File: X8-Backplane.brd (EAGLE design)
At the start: 122.1 x 106.6 mm, 13 parts, among them IC1 MAX3467CPA, U2 MIC29501-5.0WU, U3 MIC29501-5.0WU

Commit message: added some new parts
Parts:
- added U$1: MAX3491, BackplaneParts:MAX3491
- added U$2: BD6221, HBridge:BD6221
- added U1: BD6221FSOP, CamSensComponents:SOP8
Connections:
- new net VCC: U1.2, U1.3
- net GND: now also U1.8
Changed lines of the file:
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@@
 <element name="C7" library="SparkFun-Passives" package="0603-CAP" value="10uF" x="111.9378" y="51.1048" rot="MR180"/>
 <element name="C8" library="SparkFun-Passives" package="0603-CAP" value="0.1uF" x="113.6396" y="49.5046" rot="MR0"/>
+<element name="U$1" library="BackplaneParts" package="MAX3491" value="MAX3491" x="-7.112" y="-66.7512"/>
+<element name="U1" library="CamSensComponents" package="SOP8" value="BD6221FSOP" x="-15.0114" y="-65.3796"/>
+<element name="U$2" library="HBridge" package="BD6221" value="BD6221" x="-21.1074" y="-65.7606"/>
 </elements>
 <signals>
@@
 <vertex x="123.7234" y="63.0174"/>
 </polygon>
+<contactref element="U1" pad="8"/>
+<wire x1="-3.2512" y1="-48.0822" x2="-14.4164" y2="-60.4296" width="0" layer="19" extent="1-1"/>
 <wire x1="101.1564" y1="49.276" x2="-3.2512" y2="-48.0822" width="0" layer="19" extent="1-16"/>
 </signal>
@@
 <contactref element="U$4" pad="66"/>
 </signal>
+<signal name="VCC">
+<contactref element="U1" pad="2"/>
+<contactref element="U1" pad="3"/>
+<wire x1="-11.8764" y1="-65.9296" x2="-13.1464" y2="-65.9296" width="0" layer="19" extent="1-1"/>
+</signal>
 </signals>

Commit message: finished adding components, added descriptions of pins
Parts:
- removed IC1: MAX3467CPA, maxim:SO08
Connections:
- removed net +3V3: IC1.1
- removed net COM_A: IC1.8
- removed net COM_B: IC1.7
- removed net COM_Y: IC1.5
- removed net COM_Z: IC1.6
- removed net TETHER_RX: IC1.2
- removed net TETHER_TX: IC1.3
- net GND: no longer IC1.4
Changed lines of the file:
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@@
 <element name="U$3" library="Other" package="BNO055" value="BNO055_9DOF_BREAKOUT" x="21.844" y="25.146"/>
 <element name="U$4" library="backplane_to_shield_connector" package="MA20-2" value="SHIELDCONNECTOR" x="60.706" y="40.894"/>
-<element name="IC1" library="maxim" package="SO08" value="MAX3467CPA" x="-5.1562" y="-45.0088">
-<attribute name="OC_NEWARK" value="unknown" x="-14.2494" y="-28.6258" size="1.778" layer="27" display="off"/>
-<attribute name="MPN" value="" x="-14.2494" y="-28.6258" size="1.778" layer="27" display="off"/>
-<attribute name="OC_FARNELL" value="unknown" x="-14.2494" y="-28.6258" size="1.778" layer="27" display="off"/>
-<attribute name="MF" value="" x="-14.2494" y="-28.6258" size="1.778" layer="27" display="off"/>
-</element>
 <element name="U$7" library="test_lib" package="MSOP_10" value="PCA9615" x="-7.9248" y="-54.991"/>
 <element name="U2" library="LDO" package="TO-263-5" value="MIC29501-5.0WU" x="101.1682" y="62.9158" rot="MR0">
@@
 </signal>
 <signal name="GND">
-<contactref element="IC1" pad="4"/>
 <contactref element="U2" pad="3"/>
 <contactref element="U3" pad="3"/>
@@
 </polygon>
 <contactref element="U1" pad="8"/>
-<wire x1="-3.2512" y1="-48.0822" x2="-14.4164" y2="-60.4296" width="0" layer="19" extent="1-1"/>
-<wire x1="101.1564" y1="49.276" x2="-3.2512" y2="-48.0822" width="0" layer="19" extent="1-16"/>
+<wire x1="101.1682" y1="65.659" x2="112.7506" y2="65.7098" width="0" layer="19" extent="16-16"/>
+<wire x1="112.7506" y1="53.9115" x2="112.7506" y2="65.7098" width="0" layer="19" extent="16-16"/>
+<wire x1="112.7878" y1="51.1048" x2="112.7506" y2="53.9115" width="0" layer="19" extent="16-16"/>
+<wire x1="112.7896" y1="49.5046" x2="112.7878" y2="51.1048" width="0" layer="19" extent="16-16"/>
+<wire x1="101.1682" y1="53.8607" x2="112.7506" y2="53.9115" width="0" layer="19" extent="16-16"/>
+<wire x1="101.1292" y1="51.0032" x2="101.1682" y2="53.8607" width="0" layer="19" extent="16-16"/>
+<wire x1="101.1564" y1="49.276" x2="101.1292" y2="51.0032" width="0" layer="19" extent="16-16"/>
+<wire x1="-14.4164" y1="-60.4296" x2="101.1564" y2="49.276" width="0" layer="19" extent="1-16"/>
 </signal>
 <signal name="+12V">
@@
 <contactref element="PCB1" pad="P$1"/>
 </signal>
-<signal name="+3V3">
-<contactref element="IC1" pad="1"/>
-</signal>
-<signal name="TETHER_RX">
-<contactref element="IC1" pad="2"/>
-</signal>
-<signal name="TETHER_TX">
-<contactref element="IC1" pad="3"/>
-</signal>
-<signal name="COM_A">
-<contactref element="IC1" pad="8"/>
-</signal>
-<signal name="COM_B">
-<contactref element="IC1" pad="7"/>
-</signal>
-<signal name="COM_Y">
-<contactref element="IC1" pad="5"/>
-</signal>
-<signal name="COM_Z">
-<contactref element="IC1" pad="6"/>
-</signal>
 <signal name="EN1">

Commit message: first draft of the sechematic. Almost there!
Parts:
- removed U$2: BD6221, HBridge:BD6221
- added U$5: AP2210, PowerComponents:SOT-23-3
- added U4, U5: FQB27P06, CamSensComponents:TO263-3
- moved U$7 112.4 mm to (13.3, 55.4), flipped to the bottom, turned to 270 degrees
- moved U$1 109.0 mm to (18.0, 39.3), flipped to the bottom
- moved U1 96.0 mm to (16.2, 25.5)
- moved U$3 37.4 mm to (22.0, 62.5), turned to 180 degrees
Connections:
- removed net N$4: PCB1.P$1
- removed net VCC: U1.2, U1.3
- new net !RE: PCB1.P$16, U$1.!RE
- new net 3.3V: U$1.VCC13, U$1.VCC14, U$3.VIN, U$5.VOUT, U$7.1, U$7.10
- new net 3V3_PIEZO: U$4.10, U$4.9, U1.1
- new net A: U$1.A, U$4.26
- new net B: U$1.B, U$4.24
- new net DE: PCB1.P$18, U$1.DE
- new net DSCLM: U$4.36, U$7.6
- new net DSCLP: U$4.35, U$7.7
- new net DSDAM: U$4.38, U$7.9
- new net DSDAP: U$4.37, U$7.8
- new net FIN: PCB1.P$33, U1.4
- new net GND_PIEZO: U$4.11, U$4.12, U1.7
- new net LASER_5V: U$4.57, U$4.58, U5.TAB
- new net LASER_ON: PCB1.P$29, U5.1
- new net LED_5V: U$4.59, U$4.60, U4.TAB
- new net LED_ON: PCB1.P$31, U4.1
- new net RIN: U1.5
- new net RX: PCB1.P$10, U$1.R0
- new net SCL: PCB1.P$5, U$3.SCL, U$4.39, U$7.4
- new net SDA: PCB1.P$3, U$3.SDA, U$4.40, U$7.2
- new net SERVO_PWM: PCB1.P$12, U$4.30
- new net TX: PCB1.P$8, U$1.DI
- new net Y: U$1.Y, U$4.20
- new net Z: U$1.Z, U$4.22
- net +12V: now also U$4.66, U$4.67, U$4.68, U1.2, U1.3, U1.6
- net +5V: now also PCB1.P$2, PCB1.P$4, U$5.VIN; no longer U$4.59, U$4.60, U$4.61, U$4.62
- net +5V_CAMERA_TUBE: now also U$4.53, U$4.54, U$4.55, U$4.56, U4.3, U5.3; no longer U$4.65, U$4.66, U$4.67, U$4.68
- net GND: now also PCB1.P$14, PCB1.P$20, PCB1.P$25, PCB1.P$30, PCB1.P$34, PCB1.P$39, PCB1.P$6, PCB1.P$9, U$1.GND6, U$1.GND7, U$3.GND, U$4.41, U$4.42, U$4.43, U$4.44, U$4.45, U$4.46, U$4.47, U$4.48, U$4.49, U$4.50, U$5.GND, U$7.5
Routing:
- added copper zone on layer 1, net GND
- removed copper zone on layer 16, net +5V
- removed copper zone on layer 16, net +5V_CAMERA_TUBE

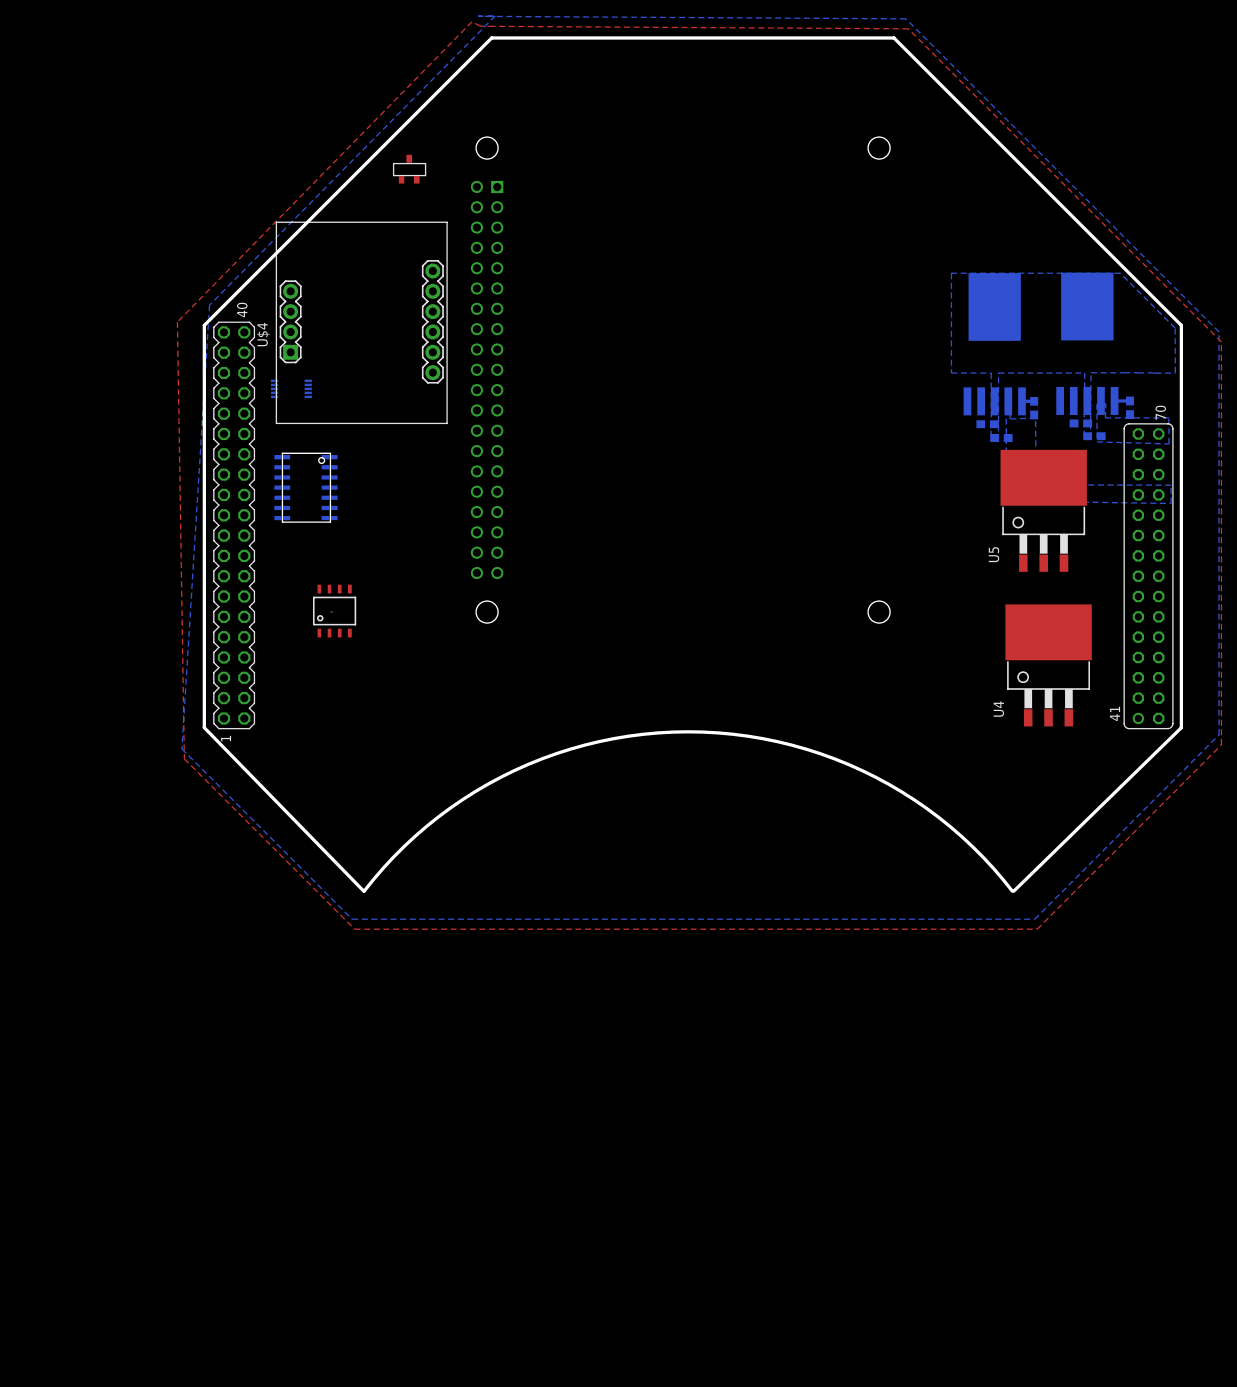
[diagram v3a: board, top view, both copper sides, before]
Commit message: Added a mosfet for an led for the blue tooth
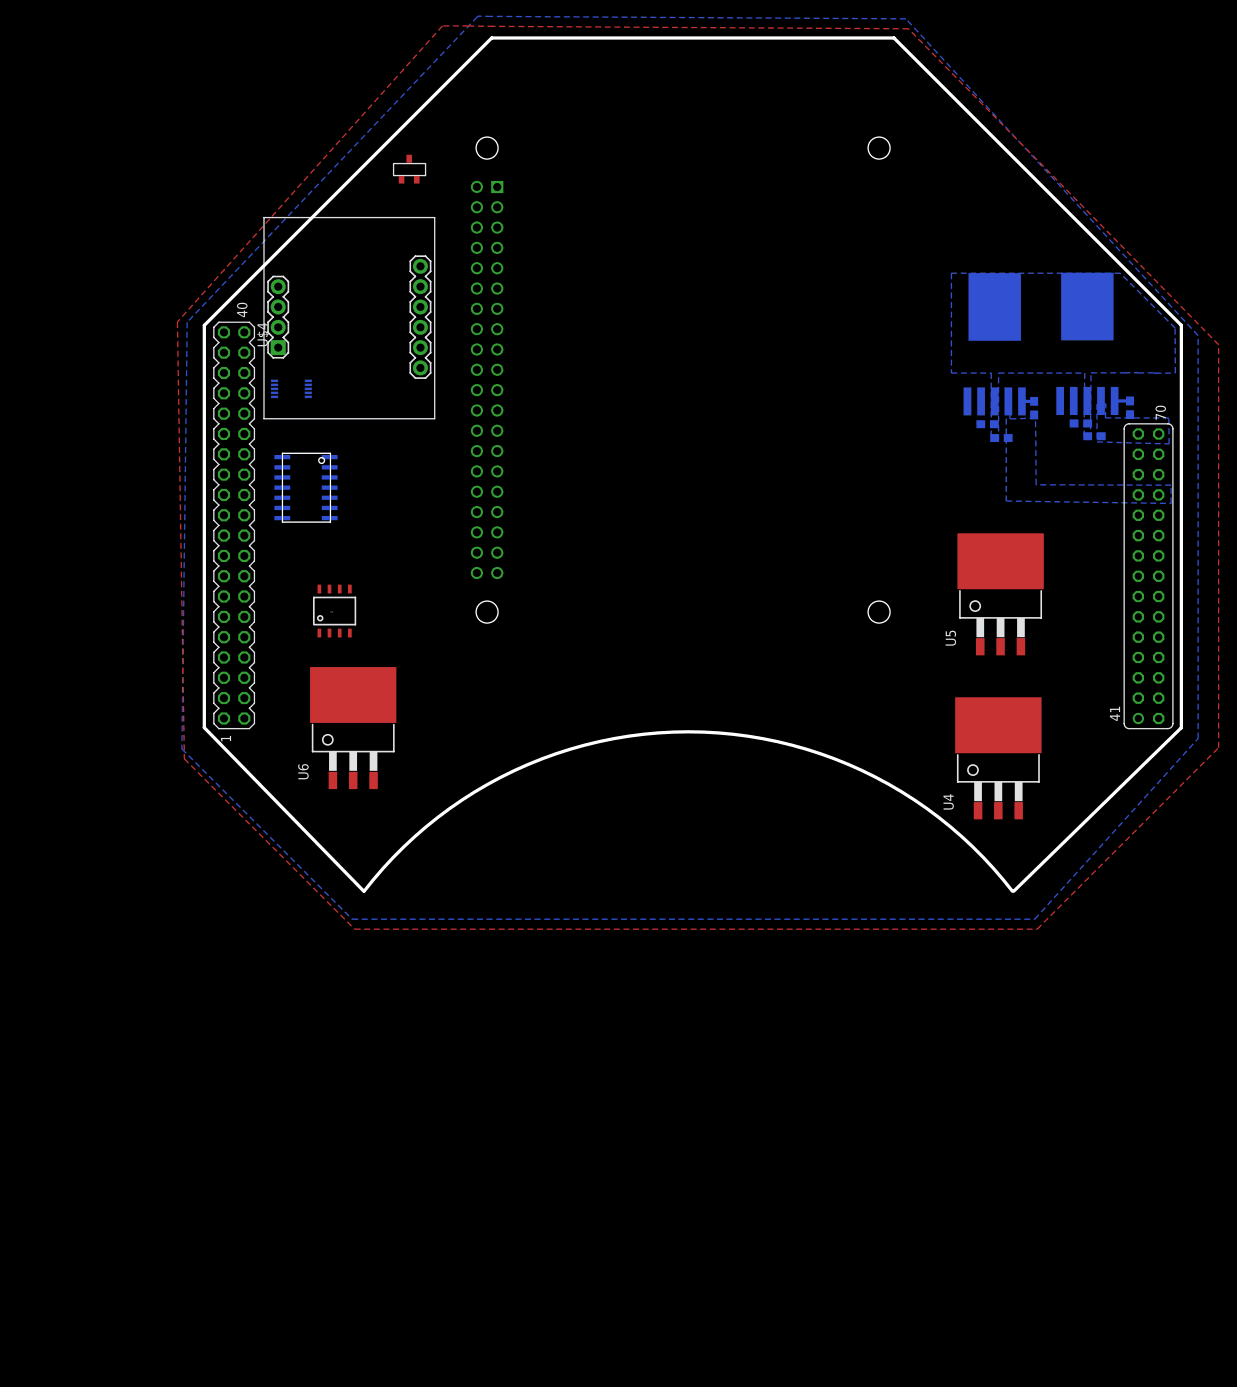
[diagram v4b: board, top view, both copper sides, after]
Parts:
- added U6: FQB27P06, CamSensComponents:TO263-3
- moved U4 13.2 mm to (101.6, 7.77)
- moved U5 11.7 mm to (101.9, 28.3)
- moved U$3 1.66 mm to (20.5, 63.1)
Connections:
- new net BT_LED_5V: U$4.15, U$4.16, U6.TAB
- new net BT_LED_ON: PCB1.P$36, U6.1
- net +5V_CAMERA_TUBE: now also U6.3
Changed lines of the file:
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@@
 <elements>
 <element name="PCB1" library="MicrocontrollerComponents" package="RPI2" value="RPI2" x="90.216" y="89.022" rot="MR270"/>
-<element name="U$3" library="Other" package="BNO055" value="BNO055_9DOF_BREAKOUT" x="22.0472" y="62.5348" rot="R180"/>
+<element name="U$3" library="Other" package="BNO055" value="BNO055_9DOF_BREAKOUT" x="20.4978" y="63.119" rot="R180"/>
 <element name="U$4" library="backplane_to_shield_connector" package="MA20-2" value="SHIELDCONNECTOR" x="60.706" y="40.894"/>
 <element name="U$7" library="test_lib" package="MSOP_10" value="PCA9615" x="13.2588" y="55.4228" rot="MR270"/>
@@
 <element name="U1" library="CamSensComponents" package="SOP8" value="BD6221FSOP" x="16.1544" y="25.4508"/>
 <element name="U$5" library="PowerComponents" package="SOT-23-3" value="AP2210" x="27.0256" y="81.5848"/>
-<element name="U4" library="CamSensComponents" package="TO263-3" value="FQB27P06" x="107.8992" y="19.3802"/>
-<element name="U5" library="CamSensComponents" package="TO263-3" value="FQB27P06" x="107.2896" y="38.7096"/>
+<element name="U4" library="CamSensComponents" package="TO263-3" value="FQB27P06" x="101.6254" y="7.7724"/>
+<element name="U5" library="CamSensComponents" package="TO263-3" value="FQB27P06" x="101.9048" y="28.2702"/>
+<element name="U6" library="CamSensComponents" package="TO263-3" value="FQB27P06" x="20.9804" y="11.557"/>
 </elements>
 <signals>
@@
 <polygon width="0.4064" layer="16">
 <vertex x="36.576" y="102.0064"/>
-<vertex x="38.735" y="102.0318"/>
-<vertex x="3.0226" y="65.8876"/>
+<vertex x="36.4998" y="101.9302"/>
+<vertex x="0.2286" y="63.754"/>
 <vertex x="-0.4318" y="10.414"/>
 <vertex x="20.8534" y="-10.8712"/>
 <vertex x="106.172" y="-10.8712"/>
-<vertex x="129.2098" y="12.1666"/>
-<vertex x="129.2098" y="62.5348"/>
+<vertex x="126.5936" y="11.7094"/>
+<vertex x="126.5936" y="62.0776"/>
 <vertex x="90.0684" y="101.6762"/>
 <vertex x="38.227" y="101.981"/>
 </polygon>
 <polygon width="0.4064" layer="1">
-<vertex x="36.8808" y="100.7618"/>
-<vertex x="35.814" y="101.2952"/>
+<vertex x="35.3822" y="100.7872"/>
+<vertex x="32.131" y="100.7872"/>
 <vertex x="-0.9906" y="63.7794"/>
 <vertex x="-0.127" y="9.1694"/>
 <vertex x="21.1582" y="-12.1158"/>
 <vertex x="106.4768" y="-12.1158"/>
-<vertex x="129.5146" y="10.922"/>
-<vertex x="129.5146" y="61.2902"/>
+<vertex x="129.159" y="10.5664"/>
+<vertex x="129.159" y="60.9346"/>
 <vertex x="90.3732" y="100.4316"/>
 <vertex x="38.5318" y="100.7364"/>
@@
 <contactref element="U$4" pad="56"/>
 <contactref element="U$4" pad="54"/>
+<contactref element="U6" pad="3"/>
 <wire x1="111.0878" y1="51.1048" x2="111.0488" y2="53.9115" width="0" layer="19" extent="16-16"/>
-<wire x1="109.8296" y1="33.6296" x2="111.0878" y2="51.1048" width="0" layer="19" extent="1-16"/>
-<wire x1="119.126" y1="32.004" x2="109.8296" y2="33.6296" width="0" layer="19" extent="1-1"/>
+<wire x1="119.126" y1="32.004" x2="111.0878" y2="51.1048" width="0" layer="19" extent="16-16"/>
 <wire x1="121.666" y1="32.004" x2="119.126" y2="32.004" width="0" layer="19" extent="1-1"/>
 <wire x1="121.666" y1="29.464" x2="121.666" y2="32.004" width="0" layer="19" extent="1-1"/>
 <wire x1="119.126" y1="29.464" x2="119.126" y2="32.004" width="0" layer="19" extent="1-1"/>
-<wire x1="110.4392" y1="14.3002" x2="119.126" y2="29.464" width="0" layer="19" extent="1-1"/>
+<wire x1="104.4448" y1="23.1902" x2="119.126" y2="29.464" width="0" layer="19" extent="1-1"/>
+<wire x1="104.1654" y1="2.6924" x2="104.4448" y2="23.1902" width="0" layer="19" extent="1-1"/>
+<wire x1="23.5204" y1="6.477" x2="104.1654" y2="2.6924" width="0" layer="19" extent="1-1"/>
 </signal>
 <signal name="3.3V">
@@
 <contactref element="U$1" pad="VCC14"/>
 <contactref element="U$1" pad="VCC13"/>
-<wire x1="30.9372" y1="57.4548" x2="28.9256" y2="81.5848" width="0" layer="19" extent="1-1"/>
-<wire x1="15.3683" y1="56.4228" x2="30.9372" y2="57.4548" width="0" layer="19" extent="16-16"/>
+<wire x1="29.3878" y1="58.039" x2="28.9256" y2="81.5848" width="0" layer="19" extent="1-1"/>
+<wire x1="15.3683" y1="56.4228" x2="29.3878" y2="58.039" width="0" layer="19" extent="16-16"/>
 <wire x1="11.1493" y1="56.4228" x2="15.3683" y2="56.4228" width="0" layer="19" extent="16-16"/>
 <wire x1="12.1155" y1="46.8884" x2="11.1493" y2="56.4228" width="0" layer="19" extent="16-16"/>
@@
 <contactref element="U$4" pad="40"/>
 <contactref element="PCB1" pad="P$3"/>
-<wire x1="30.9372" y1="65.0748" x2="38.9842" y2="78.1254" width="0" layer="19" extent="1-1"/>
-<wire x1="15.3683" y1="55.9228" x2="30.9372" y2="65.0748" width="0" layer="19" extent="16-16"/>
+<wire x1="29.3878" y1="65.659" x2="38.9842" y2="78.1254" width="0" layer="19" extent="1-1"/>
+<wire x1="15.3683" y1="55.9228" x2="29.3878" y2="65.659" width="0" layer="19" extent="16-16"/>
 <wire x1="7.366" y1="62.484" x2="15.3683" y2="55.9228" width="0" layer="19" extent="16-16"/>
 </signal>
@@
 <contactref element="U$4" pad="39"/>
 <contactref element="PCB1" pad="P$5"/>
-<wire x1="30.9372" y1="67.6148" x2="38.9842" y2="75.5854" width="0" layer="19" extent="1-1"/>
-<wire x1="15.3683" y1="54.9228" x2="30.9372" y2="67.6148" width="0" layer="19" extent="16-16"/>
+<wire x1="29.3878" y1="68.199" x2="38.9842" y2="75.5854" width="0" layer="19" extent="1-1"/>
+<wire x1="15.3683" y1="54.9228" x2="29.3878" y2="68.199" width="0" layer="19" extent="16-16"/>
 <wire x1="4.826" y1="62.484" x2="15.3683" y2="54.9228" width="0" layer="19" extent="16-16"/>
 </signal>
@@
 <contactref element="U$4" pad="60"/>
 <wire x1="119.126" y1="37.084" x2="121.666" y2="37.084" width="0" layer="19" extent="1-1"/>
-<wire x1="107.8992" y1="24.9809" x2="119.126" y2="37.084" width="0" layer="19" extent="1-1"/>
+<wire x1="101.6254" y1="13.3731" x2="119.126" y2="37.084" width="0" layer="19" extent="1-1"/>
 </signal>
 <signal name="LASER_5V">
@@
 <contactref element="U$4" pad="58"/>
 <wire x1="119.126" y1="34.544" x2="121.666" y2="34.544" width="0" layer="19" extent="1-1"/>
-<wire x1="107.2896" y1="44.3103" x2="119.126" y2="34.544" width="0" layer="19" extent="1-1"/>
+<wire x1="101.9048" y1="33.8709" x2="119.126" y2="34.544" width="0" layer="19" extent="1-1"/>
 </signal>
 <signal name="LED_ON">
 <contactref element="U4" pad="1"/>
 <contactref element="PCB1" pad="P$31"/>
-<wire x1="38.9842" y1="42.5654" x2="105.3592" y2="14.3002" width="0" layer="19" extent="1-1"/>
+<wire x1="38.9842" y1="42.5654" x2="99.0854" y2="2.6924" width="0" layer="19" extent="1-1"/>
 </signal>
 <signal name="LASER_ON">
 <contactref element="U5" pad="1"/>
 <contactref element="PCB1" pad="P$29"/>
-<wire x1="38.9842" y1="45.1054" x2="104.7496" y2="33.6296" width="0" layer="19" extent="1-1"/>
+<wire x1="38.9842" y1="45.1054" x2="99.3648" y2="23.1902" width="0" layer="19" extent="1-1"/>
 </signal>
 <signal name="DSDAM">
@@
 <wire x1="7.366" y1="49.784" x2="36.4442" y2="67.9654" width="0" layer="19" extent="1-1"/>
 </signal>
+<signal name="BT_LED_ON">
+<contactref element="U6" pad="1"/>
+<contactref element="PCB1" pad="P$36"/>
+<wire x1="18.4404" y1="6.477" x2="36.4442" y2="37.4854" width="0" layer="19" extent="1-1"/>
+</signal>
+<signal name="BT_LED_5V">
+<contactref element="U6" pad="TAB"/>
+<contactref element="U$4" pad="15"/>
+<contactref element="U$4" pad="16"/>
+<wire x1="7.366" y1="32.004" x2="20.9804" y2="17.1577" width="0" layer="19" extent="1-1"/>
+<wire x1="4.826" y1="32.004" x2="7.366" y2="32.004" width="0" layer="19" extent="1-1"/>
+</signal>
 </signals>
